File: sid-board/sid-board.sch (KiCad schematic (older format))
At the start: 13 parts, among them J1 ICM_CONN, J2 SID_CONN, J3 5V/GND, J4 3.3V/GND, J5 SPI, J6 UARTAB/IRQ, U1 SC16IS752IPW, U2 LM2596MODULE, U3 PCA82C250, U4 PCA82C250

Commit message: Happy with first prototype, going to try get it made!
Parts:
- J1, J2: footprint Connector_PinHeader_2.54mm:PinHeader_2x06_P2.54mm_Vertical -> sid-board:SAAB_SID_CONNECTOR_HEADER
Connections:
- net at J6.1 (Pin_1), U1.4 (RXA): now also U3.4 (RxD)
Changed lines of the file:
@@
 EESchema Schematic File Version 4
+LIBS:sid-board-cache
 EELAYER 30 0
 EELAYER END
@@
 F 0 "J1" H 2650 3065 50  0000 C CNN
 F 1 "ICM_CONN" H 2650 2974 50  0000 C CNN
-F 2 "Connector_PinHeader_2.54mm:PinHeader_2x06_P2.54mm_Vertical" H 2400 2600 50  0001 C CNN
+F 2 "sid-board:SAAB_SID_CONNECTOR_HEADER" H 2400 2600 50  0001 C CNN
 F 3 "~" H 2400 2600 50  0001 C CNN
 	1    2650 2600
@@
 F 0 "J2" H 2650 4065 50  0000 C CNN
 F 1 "SID_CONN" H 2650 3974 50  0000 C CNN
-F 2 "Connector_PinHeader_2.54mm:PinHeader_2x06_P2.54mm_Vertical" H 2400 3600 50  0001 C CNN
+F 2 "sid-board:SAAB_SID_CONNECTOR_HEADER" H 2400 3600 50  0001 C CNN
 F 3 "~" H 2400 3600 50  0001 C CNN
 	1    2650 3600
@@
 Wire Wire Line
 	3950 2300 3900 2300
+Wire Wire Line
+	4700 2300 4700 2350
 $EndSCHEMATC

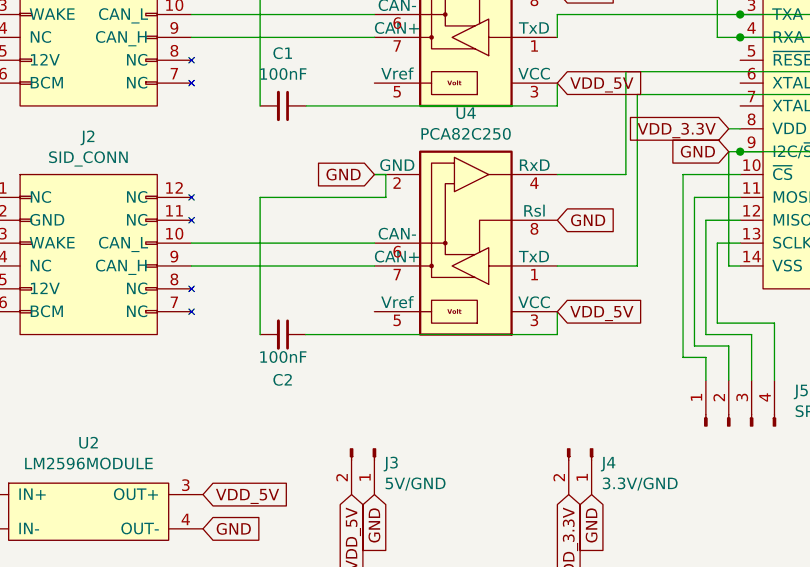
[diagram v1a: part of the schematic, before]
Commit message: Removed unnessecary cap, re-arranged.
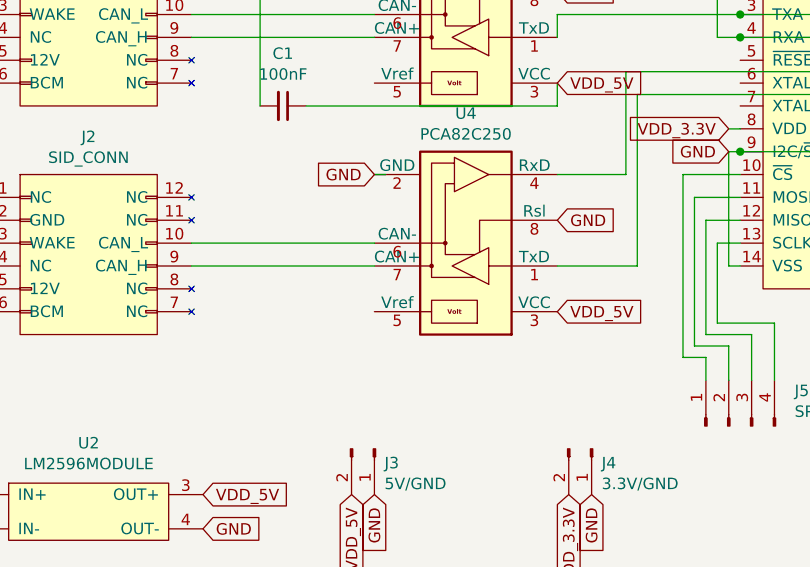
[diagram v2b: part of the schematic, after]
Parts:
- removed C2: 100nF, Capacitor_THT:C_Rect_L7.2mm_W2.5mm_P5.00mm_FKS2_FKP2_MKS2_MKP2, symbol Device:C_Small
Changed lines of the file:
@@
 EESchema Schematic File Version 4
-LIBS:sid-board-cache
 EELAYER 30 0
 EELAYER END
@@
 	0    1    1    0
 $EndComp
-$Comp
-L Device:C_Small C2
-U 1 1 5E2BBFA7
-P 3500 4000
-F 0 "C2" V 3700 4000 50  0000 C CNN
-F 1 "100nF" V 3600 4000 50  0000 C CNN
-F 2 "Capacitor_THT:C_Rect_L7.2mm_W2.5mm_P5.00mm_FKS2_FKP2_MKS2_MKP2" H 3500 4000 50  0001 C CNN
-F 3 "~" H 3500 4000 50  0001 C CNN
-	1    3500 4000
-	0    1    1    0
-$EndComp
 Wire Wire Line
 	3950 2450 3400 2450
@@
 	4700 3000 4700 2900
 Wire Wire Line
-	3400 4000 3400 3400
-Wire Wire Line
-	3400 3400 3950 3400
-Wire Wire Line
-	3950 3400 3950 3300
-Wire Wire Line
 	3950 3300 3900 3300
 Wire Wire Line
-	3600 4000 4700 4000
-Wire Wire Line
-	4700 4000 4700 3900
-Wire Wire Line
 	5450 3100 5500 3100

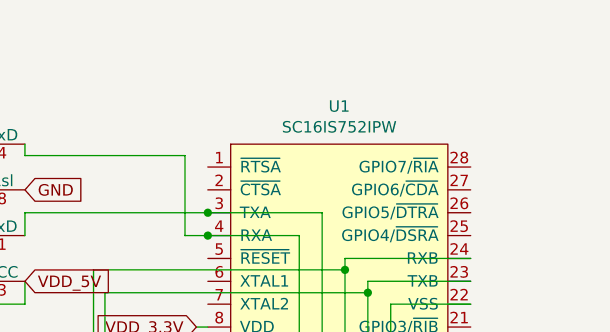
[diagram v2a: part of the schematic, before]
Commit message: Working on new mostly-SMD version, switched to independant LDOs, added oscillator circuit.
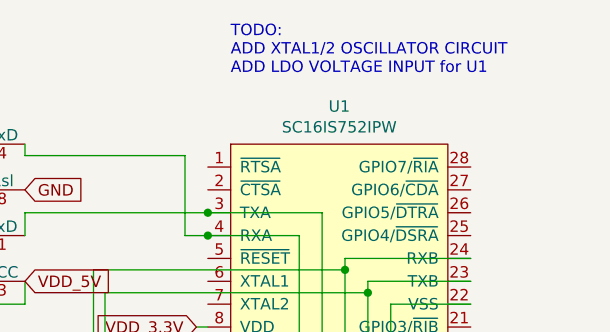
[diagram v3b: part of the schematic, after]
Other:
- note added: "TODO:\nADD XTAL1/2 OSCILLATOR CIRCUIT\nADD LDO VOLTAGE INPUT for U1"
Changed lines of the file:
@@
 Wire Wire Line
 	4700 2300 4700 2350
+Text Notes 5600 2000 0    50   ~ 0
+TODO:\nADD XTAL1/2 OSCILLATOR CIRCUIT\nADD LDO VOLTAGE INPUT for U1
 $EndSCHEMATC
